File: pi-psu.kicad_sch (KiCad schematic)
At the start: 19 parts, among them Q1 j113, Q2 PNP, Q3 NPN

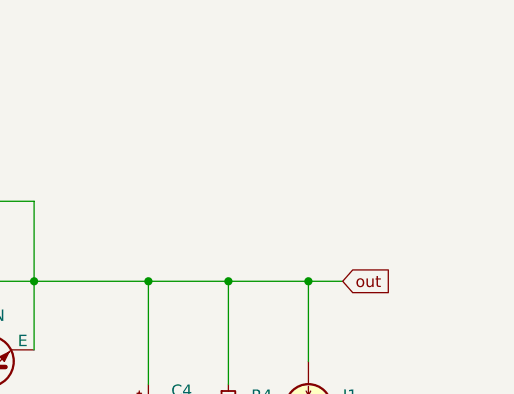
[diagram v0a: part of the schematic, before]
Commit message: made power traces 4mm
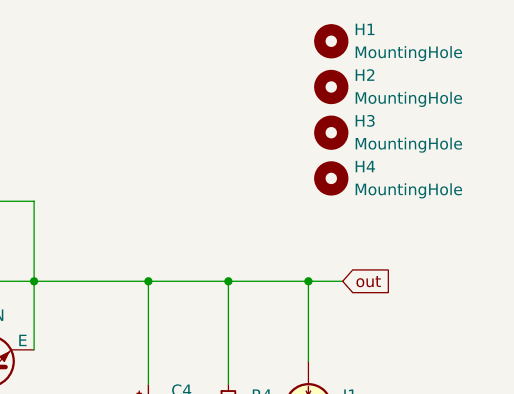
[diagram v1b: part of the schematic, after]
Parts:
- added H1, H2, H3, H4: MountingHole, MountingHole:MountingHole_3.2mm_M3_ISO7380, symbol Mechanical:MountingHole

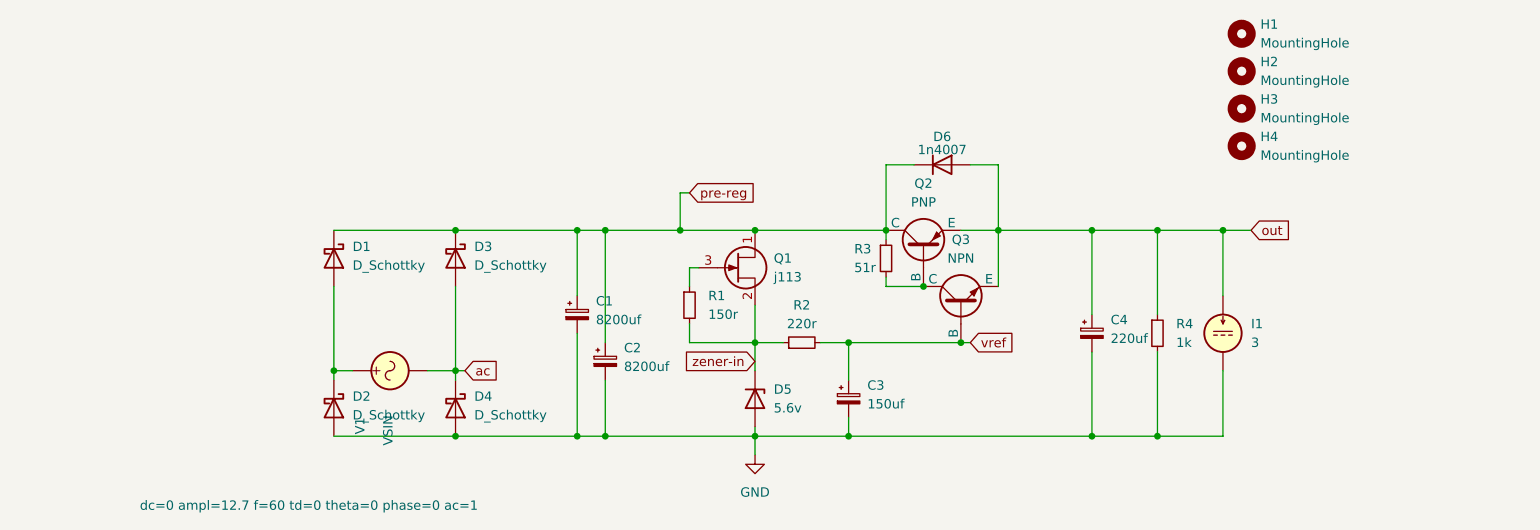
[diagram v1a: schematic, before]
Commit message: doenst work with tip41 and 41
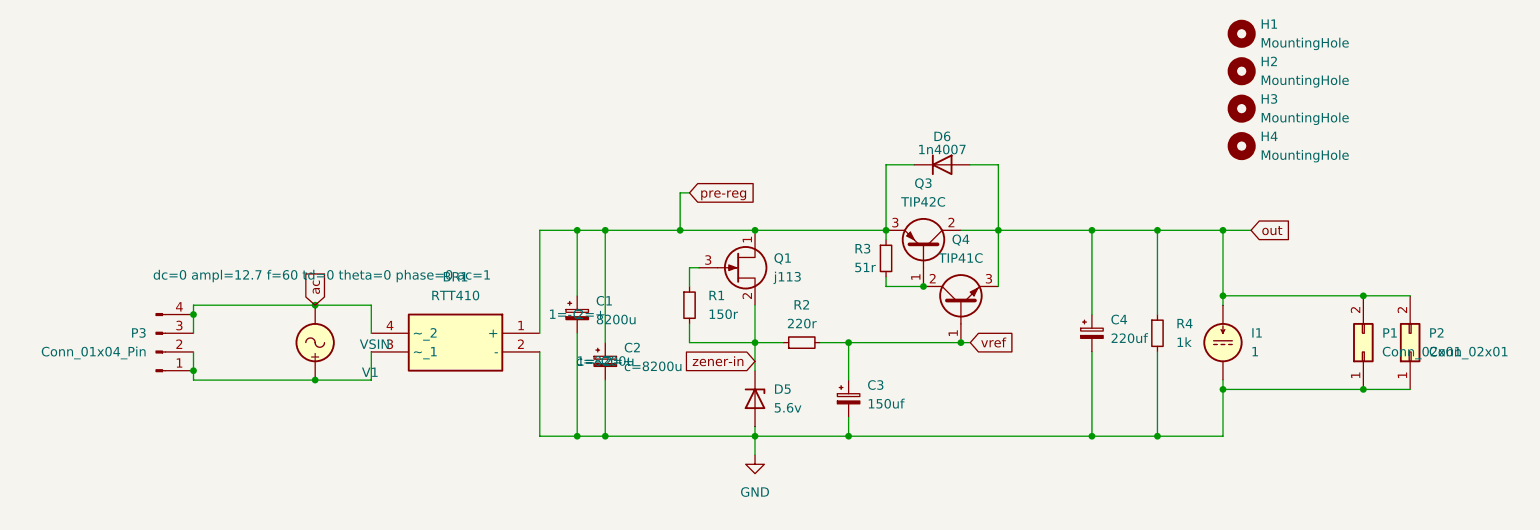
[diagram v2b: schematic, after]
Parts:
- removed D1, D2, D3, D4: D_Schottky, Diode_SMD:D_SMC, symbol Device:D_Schottky
- removed Q2: PNP, Package_TO_SOT_THT:TO-3P-3_Horizontal_TabDown, symbol Simulation_SPICE:PNP
- removed Q3: NPN, Package_TO_SOT_THT:TO-220-3_Vertical, symbol Simulation_SPICE:NPN
- added BR1: RTT410, Samacsys:SOP500P990X180-4N, symbol Samacsys:RTT410
- added P1, P2: Conn_02x01, Connector_PinHeader_2.54mm:PinHeader_1x02_P2.54mm_Vertical, symbol Connector_Generic:Conn_02x01
- added P3: Conn_01x04_Pin, Connector_Samtec_HPM_THT:Samtec_HPM-04-01-x-S_Straight_1x04_Pitch5.08mm, symbol Connector:Conn_01x04_Pin
- added Q3: TIP42C, Package_TO_SOT_THT:TO-220-3_Horizontal_TabDown, symbol Transistor_BJT:TIP42C
- added Q4: TIP41C, Package_TO_SOT_THT:TO-220-3_Horizontal_TabDown, symbol Transistor_BJT:TIP41C
- C1: value 8200uf -> 8200u
- C2: value 8200uf -> ${SIM.PARAMS}
- I1: value 3 -> 1; footprint Samacsys:395443002 -> (none)
- V1: footprint Samacsys:395443002 -> Connector_Samtec_HPM_THT:Samtec_HPM-04-01-x-S_Straight_1x04_Pitch5.08mm
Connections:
- net GND: now also BR1.2 (-), P1.1 (Pin_1), P2.1 (Pin_1)
- net ac: now also BR1.4 (~_2), P3.3 (Pin_3), P3.4 (Pin_4)
- net out: now also P1.2 (Pin_2), P2.2 (Pin_2), Q3.2 (C), Q4.3 (E)
- net pre-reg: now also BR1.1 (+), Q3.3 (E)
- net vref: now also Q4.1 (B)
- net at V1.1: now also BR1.3 (~_1), P3.1 (Pin_1), P3.2 (Pin_2)
- net at R3.2: now also Q3.1 (B), Q4.2 (C)
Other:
- moved on the sheet: V1

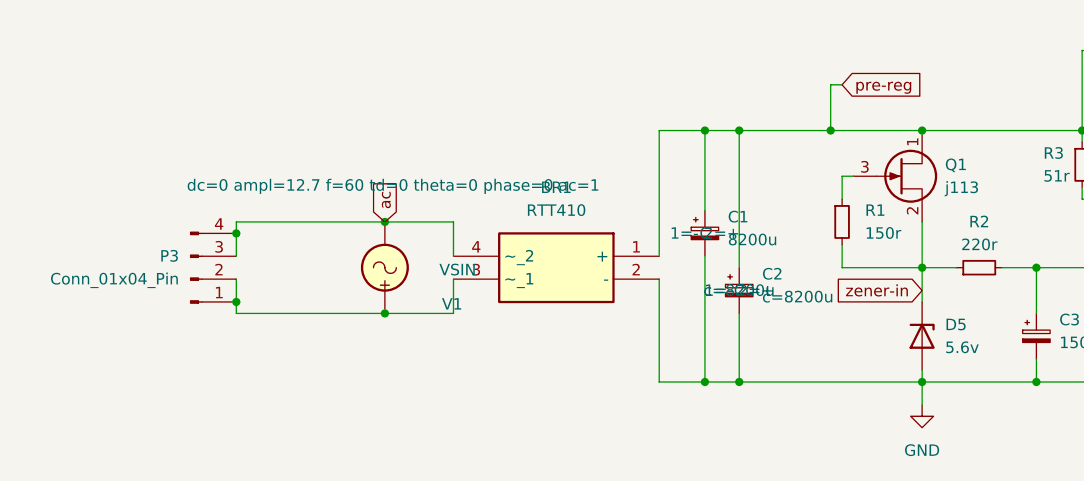
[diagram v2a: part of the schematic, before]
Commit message: sims well, sending to jlc
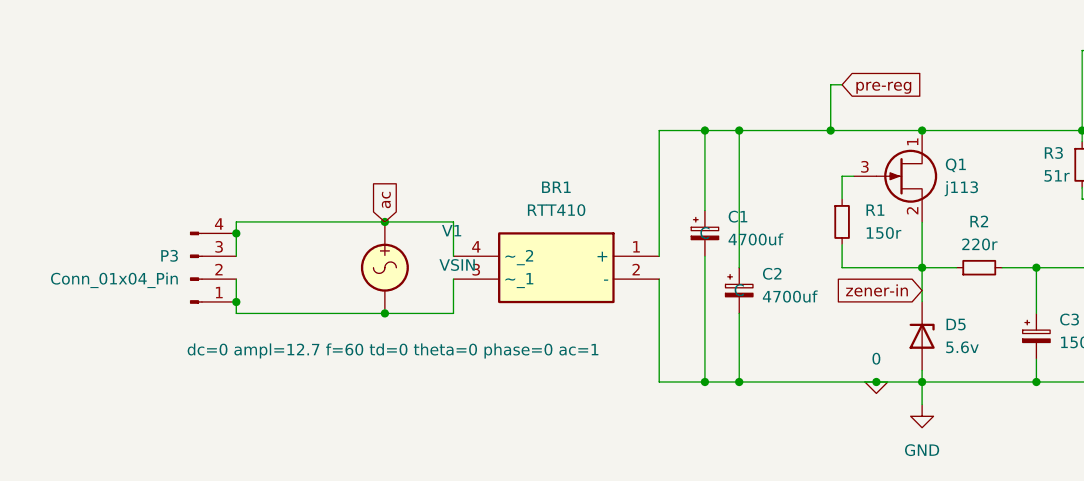
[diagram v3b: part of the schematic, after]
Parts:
- C1: value 8200u -> 4700uf; footprint Capacitor_THT:CP_Radial_D18.0mm_P7.50mm -> Capacitor_THT:CP_Radial_D12.5mm_P5.00mm
- C2: value ${SIM.PARAMS} -> 4700uf; footprint Capacitor_THT:CP_Radial_D18.0mm_P7.50mm -> Capacitor_THT:CP_Radial_D12.5mm_P5.00mm
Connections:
- net ac: now also V1.1; no longer V1.2
- net at BR1.3 (~_1), P3.1 (Pin_1), P3.2 (Pin_2): now also V1.2; no longer V1.1
- net GND renamed 0
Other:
- moved on the sheet: V1
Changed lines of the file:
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@@
+	)
+	(junction
+		(at 139.7 99.06)
+		(diameter 0)
+		(color 0 0 0 0)
 	)
 	(junction
@@
 	(wire
 		(pts
+			(xy 144.78 99.06) (xy 157.48 99.06)
+		)
+		(stroke
+			(width 0)
+			(type default)
+		)
+	)
+	(wire
+		(pts
 			(xy 135.89 66.04) (xy 134.62 66.04)
 		)
@@
 	(wire
 		(pts
-			(xy 124.46 99.06) (xy 144.78 99.06)
+			(xy 124.46 99.06) (xy 139.7 99.06)
 		)
 		(stroke
@@
 	(wire
 		(pts
-			(xy 144.78 99.06) (xy 157.48 99.06)
-		)
-		(stroke
-			(width 0)
-			(type default)
-		)
-	)
-	(wire
-		(pts
 			(xy 85.09 81.28) (xy 92.71 81.28)
 		)
@@
 		(pts
 			(xy 115.57 71.12) (xy 120.65 71.12)
+		)
+		(stroke
+			(width 0)
+			(type default)
+		)
+	)
+	(wire
+		(pts
+			(xy 139.7 99.06) (xy 144.78 99.06)
 		)
 		(stroke
@@
 	)
 	(symbol
+		(lib_id "Simulation_SPICE:0")
+		(at 139.7 99.06 0)
+		(unit 1)
+		(exclude_from_sim no)
+		(in_bom yes)
+		(on_board yes)
+		(dnp no)
+		(fields_autoplaced yes)
+		(property "Reference" "#GND02"
+			(at 139.7 104.14 0)
+			(effects
+				(font
+					(size 1.27 1.27)
+				)
+				(hide yes)
+			)
+		)
+		(property "Value" "0"
+			(at 139.7 96.52 0)
+			(effects
+				(font
+					(size 1.27 1.27)
+				)
+			)
+		)
+		(property "Footprint" ""
+			(at 139.7 99.06 0)
+			(effects
+				(font
+					(size 1.27 1.27)
+				)
+				(hide yes)
+			)
+		)
+		(property "Datasheet" "https://ngspice.sourceforge.io/docs/ngspice-html-manual/manual.xhtml#subsec_Circuit_elements__device"
+			(at 139.7 109.22 0)
+			(effects
+				(font
+					(size 1.27 1.27)
+				)
+				(hide yes)
+			)
+		)
+		(property "Description" "0V reference potential for simulation"
+			(at 139.7 106.68 0)
+			(effects
+				(font
+					(size 1.27 1.27)
+				)
+				(hide yes)
+			)
+		)
+		(pin "1"
+		)
+		(instances
+			(project ""
+				(path "/1b740d84-a3a9-471b-a0d2-626397f224fb"
+					(reference "#GND02")
+					(unit 1)
+				)
+			)
+		)
+	)
+	(symbol
 		(lib_id "Device:C_Polarized_Small")
 		(at 120.65 82.55 0)
@@
 		(on_board yes)
 		(dnp no)
-		(fields_autoplaced yes)
 		(property "Reference" "C1"
 			(at 123.19 80.7338 0)
@@
 			)
 		)
-		(property "Value" "8200u"
+		(property "Value" "4700uf"
 			(at 123.19 83.2738 0)
 			(effects
@@
 			)
 		)
-		(property "Footprint" "Capacitor_THT:CP_Radial_D18.0mm_P7.50mm"
+		(property "Footprint" "Capacitor_THT:CP_Radial_D12.5mm_P5.00mm"
 			(at 120.65 82.55 0)
 			(effects
@@
 			)
 		)
-		(property "Sim.Pins" "1=- 2=+"
-			(at 120.65 82.55 0)
+		(property "Sim.Pins" ""
+			(at 118.364 78.232 0)
 			(effects
 				(font
@@
 	(symbol
 		(lib_id "Simulation_SPICE:VSIN")
-		(at 85.09 86.36 180)
+		(at 85.09 86.36 0)
+		(mirror y)
 		(unit 1)
 		(exclude_from_sim no)
@@
 		(dnp no)
 		(property "Reference" "V1"
-			(at 93.726 90.424 0)
+			(at 93.726 82.296 0)
 			(effects
 				(font
@@
 		)
 		(property "Value" "VSIN"
-			(at 95.25 86.614 0)
+			(at 95.25 86.106 0)
 			(effects
 				(font
@@
 		)
 		(property "Sim.Params" "dc=0 ampl=12.7 f=60 td=0 theta=0 phase=0 ac=1"
-			(at 108.966 77.216 0)
+			(at 108.966 95.504 0)
 			(effects
 				(font
@@
 		(on_board yes)
 		(dnp no)
-		(fields_autoplaced yes)
 		(property "Reference" "C2"
 			(at 127 87.0838 0)
@@
 			)
 		)
-		(property "Value" "${SIM.PARAMS}"
+		(property "Value" "4700uf"
 			(at 127 89.6238 0)
 			(effects
@@
 			)
 		)
-		(property "Footprint" "Capacitor_THT:CP_Radial_D18.0mm_P7.50mm"
+		(property "Footprint" "Capacitor_THT:CP_Radial_D12.5mm_P5.00mm"
 			(at 124.46 88.9 0)
 			(effects
@@
 			)
 		)
-		(property "Sim.Params" "c=8200u"
-			(at 124.46 88.9 0)
-			(effects
-				(font
-					(size 1.27 1.27)
-				)
-			)
-		)
-		(property "Sim.Pins" "1=- 2=+"
-			(at 124.46 88.9 0)
-			(effects
-				(font
+		(property "Sim.Pins" ""
+			(at 123.698 91.44 0)
+			(effects
+				(font
